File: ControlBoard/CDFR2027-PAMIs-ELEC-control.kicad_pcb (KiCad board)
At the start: 4 copper layers, 109.8 x 79.6 mm, 89 parts, among them J1 Conn_01x04_Pin, Q1 PMOS, U1 USBLC6-2P6

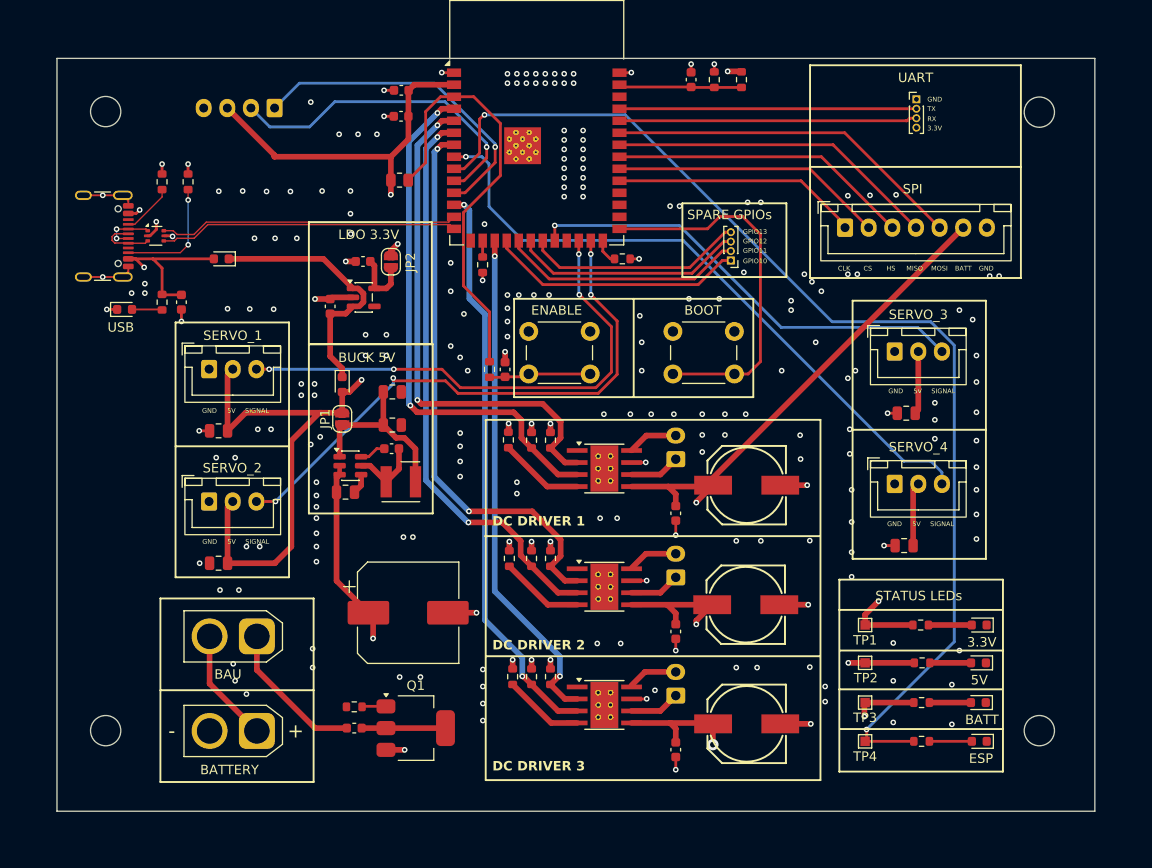
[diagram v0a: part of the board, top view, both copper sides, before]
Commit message: (change): buck 2A -> 3A (from 63200 to 63300)
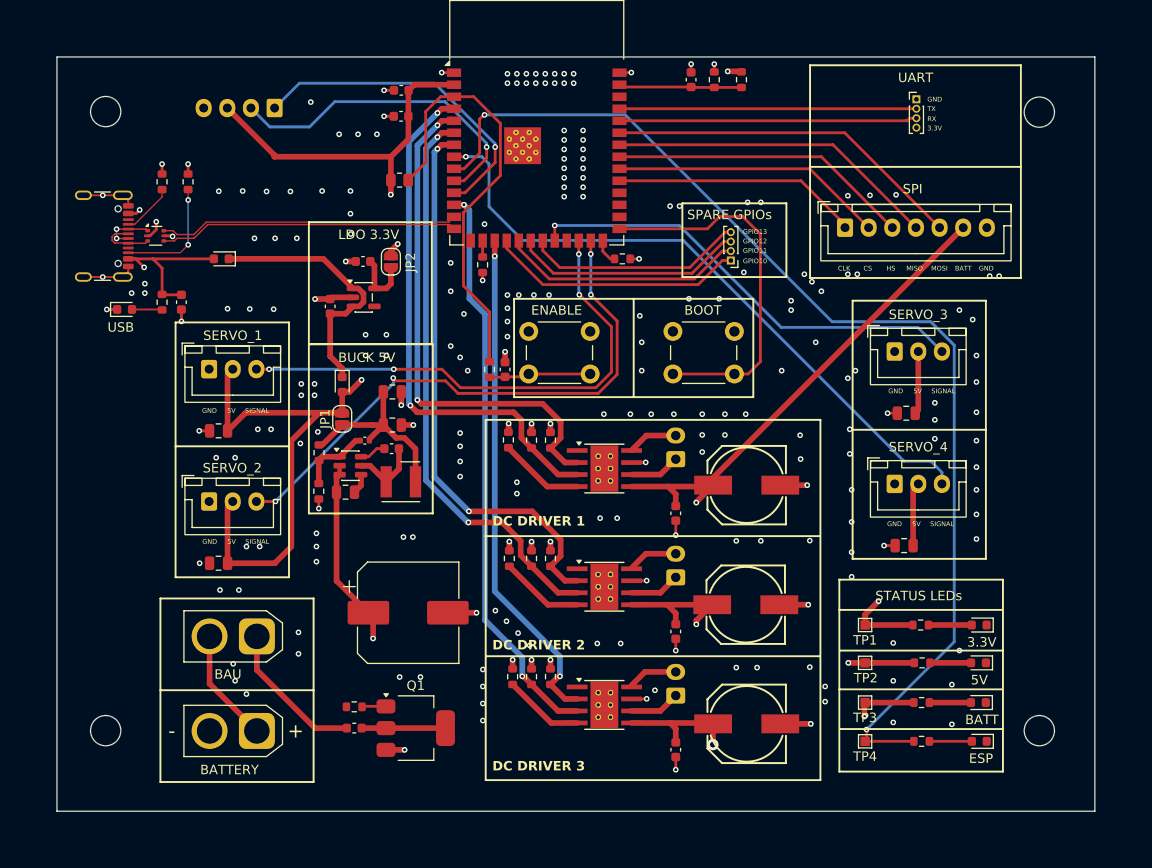
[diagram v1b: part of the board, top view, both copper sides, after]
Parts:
- added C19: 47pF, Capacitor_SMD:C_0402_1005Metric, F.Cu at (107.9, 102.8)
- added R18: 150k, PCM_SparkFun-Resistor:R_0603_1608Metric, F.Cu at (103.1, 104.1)
- added R19: 30.1k, PCM_SparkFun-Resistor:R_0603_1608Metric, F.Cu at (103.0, 108.2)
- BUCK1: value AP63205WU -> AP63300
- L1: value 4.7µH -> 6.8µH
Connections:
- C8 pad 1: Net-(BUCK1-FB) -> Net-(JP1-A)
- C9 pad 1: Net-(BUCK1-FB) -> Net-(JP1-A)
- JP1 pad 1: Net-(BUCK1-FB) -> Net-(JP1-A)
- L1 pad 2: Net-(BUCK1-FB) -> Net-(JP1-A)
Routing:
- net Net-(JP1-A): track 0.00 -> 21.4 mm
- net Net-(BUCK1-FB): track 19.2 -> 7.67 mm
- net GND: track 67.2 -> 70.9 mm, vias 227 -> 230
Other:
- board size 109.8 x 79.6 mm -> 109.8 x 79.8 mm

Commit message: (cleanup): gain space
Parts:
- moved R21 13.5 mm to (100.0, 75.7)
- moved R22 13.5 mm to (102.8, 75.7)
- moved C18 13.4 mm to (102.0, 87.8)
- moved USB_C1 13.4 mm to (92.7, 80.8)
- moved R20 13.4 mm to (99.9, 87.8)
- moved U1 13.4 mm to (99.2, 80.8)
- moved USB1 13.4 mm to (95.9, 88.5)
- moved D2 8.90 mm to (101.6, 84.2)
- moved H3 5.12 mm to (85.3, 135.2)
- moved H1 5.10 mm to (85.3, 66.3)
- moved REF** 3.09 mm to (163.2, 128.8)
- moved BAU1 2.85 mm to (99.3, 123.1)
- moved C_BATT1 2.85 mm to (99.3, 133.1)
- moved H4 2.36 mm to (177.7, 135.2)
- moved H2 2.34 mm to (177.7, 66.3)
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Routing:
- net /External IO/USB_D-: track 31.6 -> 18.0 mm
- net /External IO/USB_D+: track 31.6 -> 18.0 mm
- net Net-(D1-K): track 27.9 -> 18.8 mm
- net BATT: track 304.9 -> 311.1 mm
- net USB: track 30.0 -> 24.5 mm
- net GND: track 70.9 -> 66.7 mm, vias 230 -> 204
- net /External IO/Handshake: track 32.0 -> 30.0 mm
- net /External IO/MOSI: track 38.0 -> 36.1 mm
- net /External IO/CS: track 28.9 -> 27.0 mm
- net /External IO/SDA: track 34.6 -> 32.7 mm
- net /External IO/SCL: track 34.7 -> 32.8 mm
- net /External IO/CLK: track 26.1 -> 24.2 mm
- net /External IO/TXD0: track 31.4 -> 29.6 mm
- net Net-(BAU1-Pin_1): track 15.6 -> 14.0 mm
- net /External IO/MISO: track 35.0 -> 33.4 mm
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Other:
- board size 109.8 x 79.8 mm -> 100 x 77 mm

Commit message: (cleanup): rounded corners and gain even more space
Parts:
- moved C18 5.26 mm to (96.7, 87.8)
- moved D2 5.26 mm to (96.4, 84.2)
- moved R20 5.26 mm to (94.7, 87.8)
- moved R21 5.26 mm to (94.7, 75.7)
- moved R22 5.26 mm to (97.5, 75.7)
- moved U1 5.26 mm to (94.0, 80.8)
- moved USB1 5.26 mm to (90.7, 88.5)
- moved USB_C1 5.26 mm to (87.4, 80.8)
- moved H3 2.21 mm to (87.5, 135.4)
- moved H1 2.20 mm to (87.5, 66.3)
- moved H4 0.76 mm to (176.9, 135.4)
- moved H2 0.75 mm to (176.9, 66.3)
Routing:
- net Net-(D1-K): track 18.8 -> 24.1 mm
- net /External IO/USB_D+: track 18.0 -> 23.3 mm
- net /External IO/USB_D-: track 18.0 -> 23.3 mm
- net GND: track 66.7 -> 69.4 mm, vias 204 -> 210
- net Net-(USB_C1-CC2): track 11.9 -> 11.3 mm
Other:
- board size 100 x 77 mm -> 96.8 x 76.6 mm

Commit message: (feat): bom
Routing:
- net GND: track 69.4 -> 68.3 mm, vias 210 -> 208
- net BATT: track 311.1 -> 310.3 mm
- net Net-(BAU1-Pin_1): track 14.0 -> 14.6 mm

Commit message: (feat): routing v2
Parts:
- C13, C15, C17, C7: footprint Capacitor_SMD:C_0603_1608Metric -> Capacitor_SMD:C_0805_2012Metric
- C19: footprint Capacitor_SMD:C_0402_1005Metric -> Capacitor_SMD:C_0805_2012Metric
- R10, R11, R12, R13, R14, R15, R16, R17, R5, R9: footprint Resistor_SMD:R_0603_1608Metric -> Resistor_SMD:R_0805_2012Metric
- R18, R19: footprint PCM_SparkFun-Resistor:R_0603_1608Metric -> Resistor_SMD:R_0805_2012Metric
- moved H4 97.0 mm to (93.6, 85.7)
- moved I2C1 85.5 mm to (152.2, 135.5)
- moved H3 83.9 mm to (155.1, 85.7)
- moved H2 80.7 mm to (155.1, 144.0)
- moved H1 77.9 mm to (93.6, 144.0)
- moved SERVO_4 47.6 mm to (116.8, 113.5)
- moved C23 45.1 mm to (120.0, 118.5), turned to 0 degrees
- moved REF** 43.7 mm to (124.5, 108.6)
- moved C21 43.4 mm to (136.2, 107.5), turned to 0 degrees
- moved SERVO_2 40.4 mm to (132.5, 102.5)
- moved R1 39.8 mm to (156.2, 114.0), turned to 0 degrees
- moved C1 39.4 mm to (156.2, 116.0), turned to 180 degrees
- moved SERVO_3 37.3 mm to (132.5, 113.5)
- moved C22 34.6 mm to (136.1, 118.5), turned to 0 degrees
- moved UART1 31.0 mm to (138.8, 84.2), turned to 90 degrees
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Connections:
- net Net-(U1-I/O1-Pad1) renamed /External IO/D-
- net Net-(U1-I/O2-Pad3) renamed /External IO/D+
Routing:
- net +3.3V: track 179.3 -> 106.9 mm, vias 3 -> 2
- net BATT: track 310.3 -> 245.7 mm
- net +5V: track 176.1 -> 119.9 mm, vias 2 -> 3
- net /Actuators & Utility/SERVO_2: track 60.4 -> 13.0 mm, vias 4 -> 0
- net /Actuators & Utility/SERVO_1: track 53.2 -> 11.6 mm, vias 4 -> 0
- net /Actuators & Utility/STATUS_LED: track 119.6 -> 82.1 mm
- net /External IO/SDA: track 32.7 -> 68.5 mm
- net /External IO/SCL: track 32.8 -> 68.2 mm
- net /Actuators & Utility/SERVO_4: track 69.3 -> 35.7 mm
- net /Actuators & Utility/SERVO_3: track 48.1 -> 24.0 mm
- net /Actuators & Utility/GPIO10: track 27.2 -> 3.11 mm
- net /Actuators & Utility/GPIO11: track 26.3 -> 3.00 mm
- net Net-(ESP32-S3-WROOM1-EN): track 45.9 -> 68.9 mm, vias 0 -> 2
- net /Actuators & Utility/GPIO12: track 24.7 -> 2.89 mm
- net /External IO/TXD0: track 29.6 -> 8.16 mm
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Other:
- board size 96.8 x 76.6 mm -> 80.4 x 79.8 mm
- board text added: "BUCK"
- board text added: "Carte de contrôle V2 PAMIs CDFR 2027"
- board text added: "I2C"
- board text added: "LDO"
- board text added: "SERVO 1"
- board text added: "SERVO 2"
- board text added: "SERVO 3"
- board text added: "SERVO 4"
- board text added: "SERVO PIN ORDER GND | 5V | SIGNAL"
- board text added: "SPARE GPIO"
- board text removed: "BUCK 5V"
- board text removed: "Carte de contrôle V1 PAMIs CDFR 2027"
- board text removed: "GPIO10"
- board text removed: "GPIO11"
- board text removed: "GPIO12"
- board text removed: "GPIO13"
- board text removed: "I2C OTOS"
- board text removed: "LDO 3.3V"
- board text removed: "OUT1"
- board text removed: "OUT2"
- board text removed: "SIGNAL"
- board text removed: "SPARE GPIOs"
- board text removed: "STATUS LEDs"

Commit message: Updates to PCB by Ludo <3
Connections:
- net Net-(ESP32-S3-WROOM1-EN) renamed /EN
- net Net-(ESP32-S3-WROOM1-IO0) renamed /BOOT

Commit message: (fixes): various small fixes
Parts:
- moved U1 6.68 mm to (99.5, 96.4)
- moved C3 6.15 mm to (114.2, 77.0)
- moved R21 2.57 mm to (102.1, 93.2)
- moved R22 2.07 mm to (103.0, 98.2)
- moved R2 1.61 mm to (111.0, 78.4)
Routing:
- net /External IO/D-: track 12.7 -> 5.78 mm
- net /External IO/D+: track 12.0 -> 5.27 mm
- net /External IO/USB_D-: track 11.2 -> 17.7 mm
- net /External IO/USB_D+: track 11.2 -> 17.7 mm
- net USB: track 31.9 -> 36.9 mm
- net +3.3V: track 106.9 -> 109.8 mm
- net Net-(USB_C1-CC1): track 3.42 -> 5.94 mm
- net Net-(USB_C1-CC2): track 3.52 -> 5.61 mm
- net /EN: track 68.9 -> 70.2 mm
- net GND: vias 582 -> 264

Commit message: (fix): pmos pad 4 not connected to drain
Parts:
- LED_3.3V1, LED_5V1, LED_BATT1: value LED -> RED
- USB1: value LED -> GREEN
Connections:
- Q1 pad 4: (no net) -> Net-(Q1-D)
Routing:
- net Net-(Q1-D): track 6.89 -> 16.8 mm, vias 0 -> 2
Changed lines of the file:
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@@
 			)
 		)
-		(property "Value" "LED"
+		(property "Value" "RED"
 			(at 0 1.43 90)
 			(layer "F.Fab")
@@
 			)
 		)
-		(property "Value" "LED"
+		(property "Value" "GREEN"
 			(at 0 1.43 0)
 			(layer "F.Fab")
@@
 			(layers "F.Cu" "F.Mask" "F.Paste")
 			(roundrect_rratio 0.25)
+			(net "Net-(Q1-D)")
 		)
 		(embedded_fonts no)
@@
 			)
 		)
-		(property "Value" "LED"
+		(property "Value" "RED"
 			(at 0 1.43 90)
 			(layer "F.Fab")
@@
 			)
 		)
+		(property "LCSC" "C49234152"
+			(at 0 0 0)
+			(unlocked yes)
+			(layer "F.Fab")
+			(hide yes)
+			(effects
+				(font
+					(size 1 1)
+					(thickness 0.15)
+				)
+			)
+		)
 		(sheetname "/")
 		(sheetfile "CDFR2027-PAMIs-ELEC-control.kicad_sch")
@@
 			)
 		)
+		(property "LCSC" "C49234152"
+			(at 0 0 0)
+			(unlocked yes)
+			(layer "F.Fab")
+			(hide yes)
+			(effects
+				(font
+					(size 1 1)
+					(thickness 0.15)
+				)
+			)
+		)
 		(sheetname "/")
 		(sheetfile "CDFR2027-PAMIs-ELEC-control.kicad_sch")
@@
 			)
 		)
-		(property "Value" "LED"
+		(property "Value" "RED"
 			(at 0 1.43 90)
 			(layer "F.Fab")
@@
 	)
 	(segment
+		(start 101.78 117.78)
+		(end 101.8 117.8)
+		(width 0.6)
+		(layer "F.Cu")
+		(net "Net-(Q1-D)")
+	)
+	(segment
 		(start 103.9 129.7)
 		(end 101.8 127.6)
@@
 	)
 	(segment
+		(start 101.8 124.1)
+		(end 101.8 122.59)
+		(width 1)
+		(layer "F.Cu")
+		(net "Net-(Q1-D)")
+	)
+	(segment
 		(start 103.9 130.125)
 		(end 103.9 129.7)
@@
 	)
 	(segment
+		(start 101.78 115.98)
+		(end 101.78 117.78)
+		(width 0.6)
+		(layer "F.Cu")
+		(net "Net-(Q1-D)")
+	)
+	(segment
 		(start 101.8 127.6)
 		(end 101.8 124.1)
@@
 		(net "Net-(Q1-D)")
 	)
+	(via
+		(at 101.78 122.59)
+		(size 0.6)
+		(drill 0.3)
+		(layers "F.Cu" "B.Cu")
+		(net "Net-(Q1-D)")
+	)
+	(via
+		(at 101.78 115.98)
+		(size 0.6)
+		(drill 0.3)
+		(layers "F.Cu" "B.Cu")
+		(net "Net-(Q1-D)")
+	)
+	(segment
+		(start 101.78 122.59)
+		(end 101.78 115.98)
+		(width 0.6)
+		(layer "B.Cu")
+		(net "Net-(Q1-D)")
+	)
